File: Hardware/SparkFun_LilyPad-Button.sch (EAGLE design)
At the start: 5 parts

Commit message: Initial Commit
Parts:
- removed BUTTON-, BUTTONS: SEWTAP8, LilyPad-Wearables:SEWTAP8
- removed LOGO1: LOGO-LPL, LilyPad-Wearables:LOGO-LPL
- removed S1: (no value), SparkFun:TAC_SWITCHSMD
- added FRAME2: FRAME-LETTER, SparkFun-Aesthetics:FRAME-LETTER
- added JP12, JP13: SEWTAP_MEDIUM-2SIDE, LilyPad-Wearables:SEWTAP_MEDIUM-2SIDE
- added S4: MOMENTARY-SWITCH-SPST-SMD-5.2-REDUNDANT, SparkFun-Switches:MOMENTARY-SWITCH-SPST-SMD-5.2-REDUNDANT
- U$1: value CREATIVE_COMMONS -> SPECIAL_INSTRUCTIONS-ORDERING; device SparkFun:CREATIVE_COMMONS -> SparkFun-Aesthetics:SPECIAL_INSTRUCTIONS-ORDERING
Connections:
- removed net -: BUTTON-.1, S1.4
- removed net S: BUTTONS.1, S1.2
- new net D4: JP12.1, S4.1
- new net GND: JP13.1, S4.2
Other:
- note added: "Elias Santistevan"
- note added: "LilyPad concept and shpaes by: L.Buechley and N.Seidle"
- note added: "Marshall Taylor"
- note added: "Revision By:"
- note added: "v13"
- note removed: "LilyPad - Button"
- note removed: "v12"

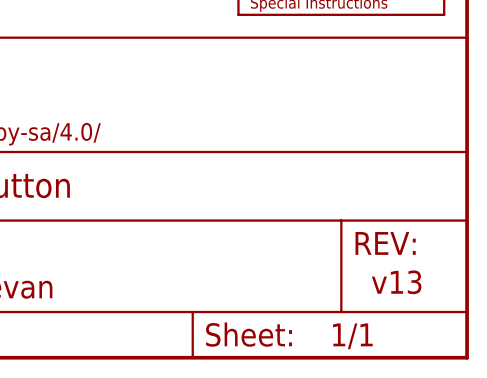
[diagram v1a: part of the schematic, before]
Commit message: Changed to v20
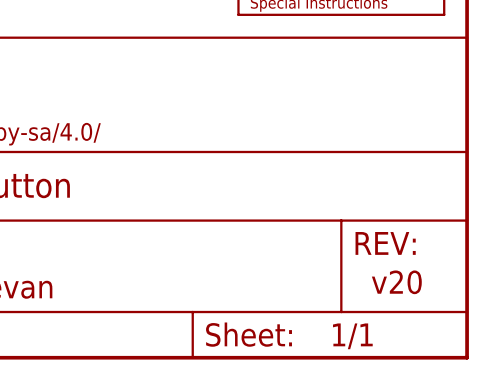
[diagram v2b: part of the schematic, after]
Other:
- note added: "v20"
- note removed: "v13"
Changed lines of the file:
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@@
 <plain>
 <text x="171.45" y="11.43" size="2.54" layer="94">Marshall Taylor</text>
-<text x="238.252" y="7.112" size="2.54" layer="94">v13</text>
+<text x="238.252" y="7.112" size="2.54" layer="94">v20</text>
 <text x="176.276" y="6.604" size="2.54" layer="94">Elias Santistevan</text>
 <text x="148.336" y="6.604" size="2.54" layer="94">Revision By:</text>
